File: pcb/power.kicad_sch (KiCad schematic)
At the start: 6 parts

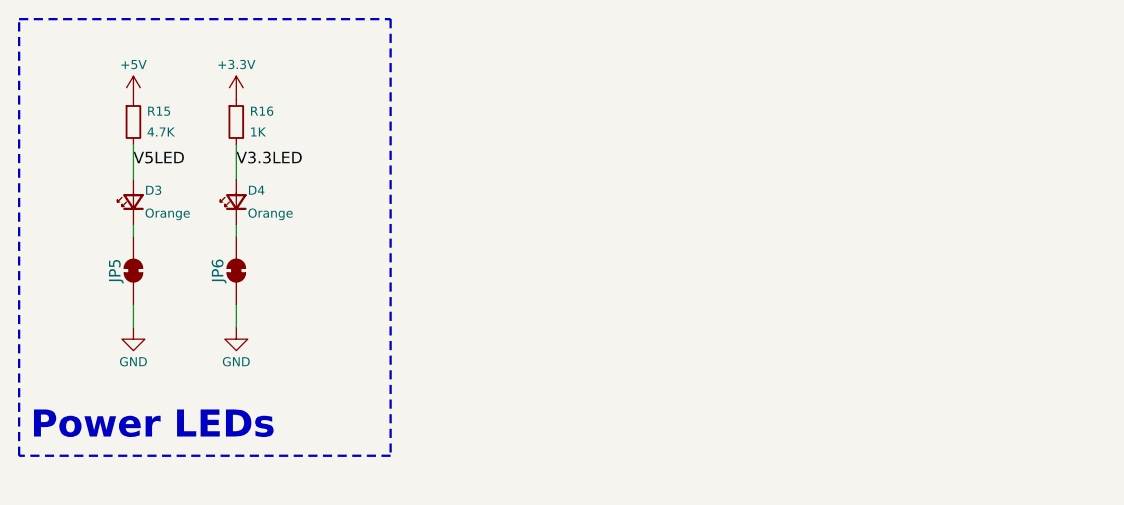
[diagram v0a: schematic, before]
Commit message: Updates for consistency
Changed mounting holes to grounded
Updated power connectors
Added power ESD protection
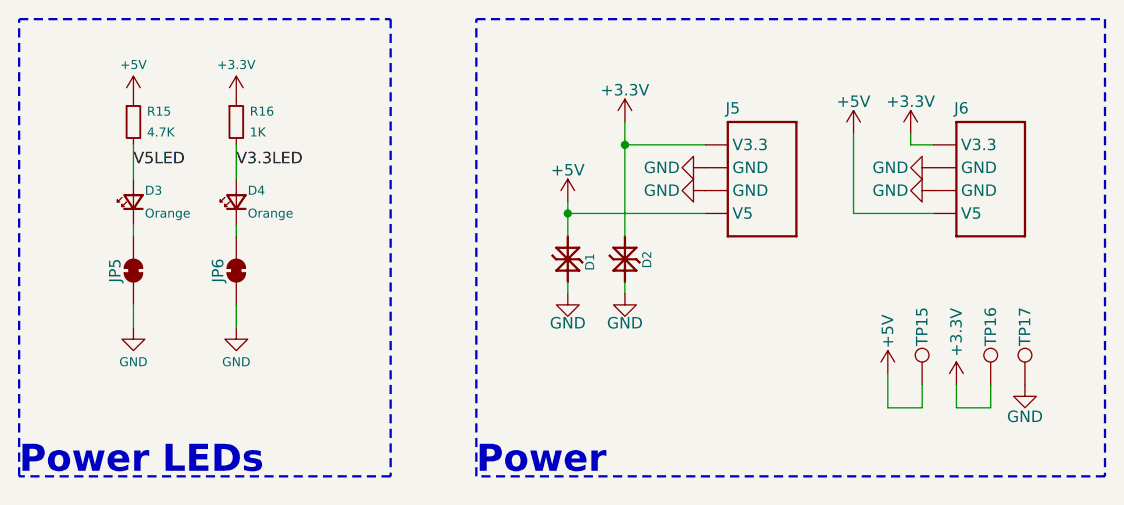
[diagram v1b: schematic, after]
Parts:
- added D1: PESD5V5C1BL, CRGM Passive:DFN1006-2, symbol CRGM Passive:PESD5V5C1BLYL
- added D2: PESD3V3S1BL, CRGM Passive:DFN1006-2, symbol CRGM Passive:PESD3V3S1BL
- added J5, J6: ~, CRGM Connector:JST_SH_SM04B-SRSS-TB_1x04-1MP_P1.00mm_Horizontal, symbol CRGM Connector:AQ_POWER
- added TP15, TP16, TP17: ~, CRGM Mechanical:TestPoint_Pad_D1.0mm, symbol Connector:TestPoint
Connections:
- net +3.3V: now also D2.2 (K2), J5.4 (V3.3), J6.4 (V3.3), TP16.1
- net +5V: now also D1.2 (K2), J5.1 (V5), J6.1 (V5), TP15.1
- net GND: now also D1.1 (K1), D2.1 (K1), J5.2 (GND), J5.3 (GND), J6.2 (GND), J6.3 (GND), TP17.1
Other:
- note added: "Power"

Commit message: Switched back to global lables
Updated all gnd and test point symbols
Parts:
- TP15, TP16, TP17: symbol Connector:TestPoint -> CRGM Connector:TestPoint
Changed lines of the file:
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@@
 			)
 		)
-		(property "Description" ""
+		(property "Description" "Power symbol creates a global label with name \"GND\" , ground"
 			(at 38.1 59.69 0)
 			(effects
@@
 	)
 	(symbol
-		(lib_id "Connector:TestPoint")
+		(lib_id "CRGM Connector:TestPoint")
 		(at 125.73 66.04 0)
 		(unit 1)
@@
 		)
 		(property "Footprint" "CRGM Mechanical:TestPoint_Pad_D1.0mm"
-			(at 130.81 66.04 0)
+			(at 125.73 73.406 0)
 			(effects
 				(font
@@
 		)
 		(property "Datasheet" "~"
-			(at 130.81 66.04 0)
-			(effects
-				(font
-					(size 1.27 1.27)
-				)
-				(hide yes)
-			)
-		)
-		(property "Description" "test point"
-			(at 125.73 66.04 0)
+			(at 128.016 64.008 0)
+			(effects
+				(font
+					(size 1.27 1.27)
+				)
+				(hide yes)
+			)
+		)
+		(property "Description" "Test Point D1.0mm"
+			(at 125.73 75.184 0)
 			(effects
 				(font
@@
 			)
 		)
-		(property "Description" ""
+		(property "Description" "Power symbol creates a global label with name \"GND\" , ground"
 			(at 49.53 59.69 0)
 			(effects
@@
 	)
 	(symbol
-		(lib_id "Connector:TestPoint")
+		(lib_id "CRGM Connector:TestPoint")
 		(at 133.35 66.04 0)
 		(unit 1)
@@
 		)
 		(property "Footprint" "CRGM Mechanical:TestPoint_Pad_D1.0mm"
-			(at 138.43 66.04 0)
+			(at 133.35 73.406 0)
 			(effects
 				(font
@@
 		)
 		(property "Datasheet" "~"
-			(at 138.43 66.04 0)
-			(effects
-				(font
-					(size 1.27 1.27)
-				)
-				(hide yes)
-			)
-		)
-		(property "Description" "test point"
-			(at 133.35 66.04 0)
+			(at 135.636 64.008 0)
+			(effects
+				(font
+					(size 1.27 1.27)
+				)
+				(hide yes)
+			)
+		)
+		(property "Description" "Test Point D1.0mm"
+			(at 133.35 75.184 0)
 			(effects
 				(font
@@
 	)
 	(symbol
-		(lib_id "Connector:TestPoint")
+		(lib_id "CRGM Connector:TestPoint")
 		(at 137.16 66.04 0)
 		(unit 1)
@@
 		)
 		(property "Footprint" "CRGM Mechanical:TestPoint_Pad_D1.0mm"
-			(at 142.24 66.04 0)
+			(at 137.16 73.406 0)
 			(effects
 				(font
@@
 		)
 		(property "Datasheet" "~"
-			(at 142.24 66.04 0)
-			(effects
-				(font
-					(size 1.27 1.27)
-				)
-				(hide yes)
-			)
-		)
-		(property "Description" "test point"
-			(at 137.16 66.04 0)
-			(effects
-				(font
+			(at 139.446 64.008 0)
+			(effects
+				(font
+					(size 1.27 1.27)
+				)
+				(hide yes)
+			)
+		)
+		(property "Description" "Test Point D1.0mm"
+			(at 137.16 75.184 0)
+			(effects
+				(font
